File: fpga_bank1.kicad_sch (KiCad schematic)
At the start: 2 parts, among them U2 XC7A50T-FGG484

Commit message: Schematic finished, starting layout
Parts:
- added C33, C40, C55, C56, C57, C59, C60, C61, C62, C63, C64: 100n, Capacitor_SMD:C_0402_1005Metric_Pad0.74x0.62mm_HandSolder, symbol Device:C_Small
- added C54, C65: 4.7u, Capacitor_SMD:C_0402_1005Metric_Pad0.74x0.62mm_HandSolder, symbol Device:C_Small
- R12: renamed from R1; footprint Resistor_SMD:R_0603_1608Metric_Pad0.98x0.95mm_HandSolder -> Resistor_SMD:R_0402_1005Metric_Pad0.72x0.64mm_HandSolder; LCSC C21190 -> (none)
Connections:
- net +3V3: now also C33.2, C40.2, C54.2, C55.2, C56.2, C57.2, C59.2, C60.2, C61.2, C62.2, C63.2, C64.2, C65.2
- net FPGA_SPI0_CE0: now reaches U2.W19 (IO_L12P_T1_MRCC_14)
- net FPGA_SPI0_CE1: now reaches U2.W20 (IO_L12N_T1_MRCC_14)
- net SPI0_SCK: now reaches U2.Y18 (IO_L13P_T2_MRCC_14)
- new net GND: C33.1, C40.1, C54.1, C55.1, C56.1, C57.1, C59.1, C60.1, C61.1, C62.1, C63.1, C64.1, C65.1
- no-connect marks 0 -> 44
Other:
- note added: "(data output for serial daisy chains)"
- note added: "(serial configuration data input)"
- note added: "Nothing specific here. On MRCC pins for just in case."
- title: FPGA Bank 14 -> FPGA Power
- moved on the sheet: R12, U2A

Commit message: Updated titleblock texts
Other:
- title: FPGA Power -> FPGA Bank 14
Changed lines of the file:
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@@
   (paper "A4")
   (title_block
-    (title "FPGA Power")
-    (date "2024-02-11")
+    (title "FPGA Bank 14")
+    (date "2024-02-14")
     (rev "0.1")
     (company "George Smart, M1GEO")

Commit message: Started routing. More to go
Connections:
- net FPGA_SPI0_CE0 renamed FPGA_PI_GPIO8
- net FPGA_SPI0_CE1 renamed FPGA_PI_GPIO7
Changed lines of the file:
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@@
     (effects (font (size 1.27 1.27)) (justify left bottom))
   )
-  (hierarchical_label "FPGA_SPI0_CE1" (shape input) (at 127 106.045 0) (fields_autoplaced)
+  (hierarchical_label "FPGA_PI_GPIO7" (shape input) (at 127 106.045 0) (fields_autoplaced)
     (effects (font (size 1.27 1.27)) (justify left))
   )
@@
     (effects (font (size 1.27 1.27)) (justify left))
   )
-  (hierarchical_label "FPGA_SPI0_CE0" (shape input) (at 127 103.505 0) (fields_autoplaced)
+  (hierarchical_label "FPGA_PI_GPIO8" (shape input) (at 127 103.505 0) (fields_autoplaced)
     (effects (font (size 1.27 1.27)) (justify left))
   )

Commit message: More routing and tinkering. Need to do non-MGT decoupling next.
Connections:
- net FPGA_PI_GPIO7: no longer names the net of U2.W20 (IO_L12N_T1_MRCC_14)
- net FPGA_PI_GPIO8: no longer names the net of U2.W19 (IO_L12P_T1_MRCC_14)
- no-connect marks 44 -> 46
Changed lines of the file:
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@@
   (no_connect (at 111.76 141.605))
   (no_connect (at 111.76 159.385))
+  (no_connect (at 111.76 103.505))
   (no_connect (at 111.76 136.525))
   (no_connect (at 111.76 118.745))
@@
   (no_connect (at 111.76 85.725))
   (no_connect (at 111.76 60.325))
+  (no_connect (at 111.76 106.045))
   (no_connect (at 111.76 111.125))
   (no_connect (at 111.76 78.105))
@@
     (stroke (width 0) (type default))
   )
-  (wire (pts (xy 111.76 108.585) (xy 127 108.585))
-    (stroke (width 0) (type default))
-  )
   (wire (pts (xy 36.83 183.515) (xy 36.83 182.245))
     (stroke (width 0) (type default))
@@
     (stroke (width 0) (type default))
   )
-  (wire (pts (xy 111.76 106.045) (xy 127 106.045))
-    (stroke (width 0) (type default))
-  )
   (wire (pts (xy 21.59 188.595) (xy 21.59 189.23))
     (stroke (width 0) (type default))
@@
     (stroke (width 0) (type default))
   )
-  (wire (pts (xy 111.76 103.505) (xy 127 103.505))
-    (stroke (width 0) (type default))
-  )
   (wire (pts (xy 41.91 188.595) (xy 41.91 189.23))
+    (stroke (width 0) (type default))
+  )
+  (wire (pts (xy 111.76 108.585) (xy 116.205 108.585))
     (stroke (width 0) (type default))
   )
@@
   )
   (text "Nothing specific here.\nOn MRCC pins for just in case."
-    (at 147.32 107.95 0)
+    (at 128.905 110.49 0)
     (effects (font (size 1.27 1.27)) (justify left bottom))
   )
@@
     (effects (font (size 1.27 1.27)) (justify left bottom))
   )
-  (hierarchical_label "FPGA_PI_GPIO7" (shape input) (at 127 106.045 0) (fields_autoplaced)
-    (effects (font (size 1.27 1.27)) (justify left))
-  )
   (hierarchical_label "FPGA_PROG_MOSI" (shape input) (at 127 50.165 0) (fields_autoplaced)
     (effects (font (size 1.27 1.27)) (justify left))
   )
-  (hierarchical_label "FPGA_PI_GPIO8" (shape input) (at 127 103.505 0) (fields_autoplaced)
-    (effects (font (size 1.27 1.27)) (justify left))
-  )
   (hierarchical_label "FPGA_PROG_MISO" (shape output) (at 127 121.285 0) (fields_autoplaced)
     (effects (font (size 1.27 1.27)) (justify left))
   )
-  (hierarchical_label "SPI0_SCK" (shape input) (at 127 108.585 0) (fields_autoplaced)
+  (hierarchical_label "SPI0_SCK" (shape input) (at 116.205 108.585 0) (fields_autoplaced)
     (effects (font (size 1.27 1.27)) (justify left))
   )

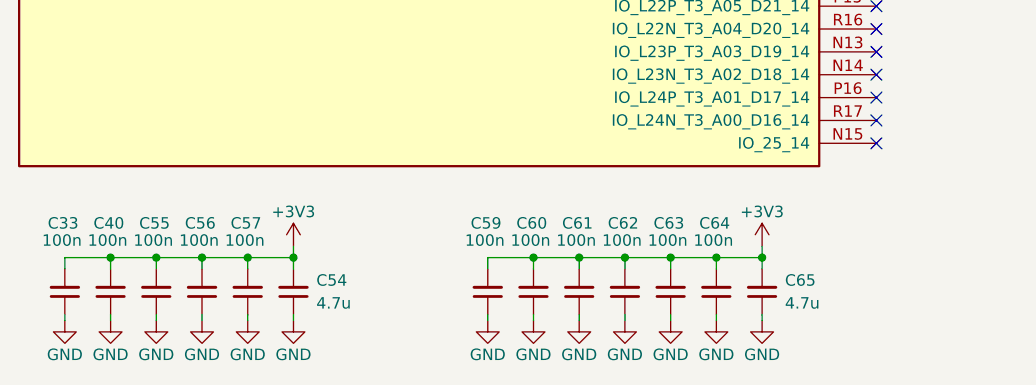
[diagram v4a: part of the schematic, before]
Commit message: Updated decoupling. Need to work out larger planes and fills.
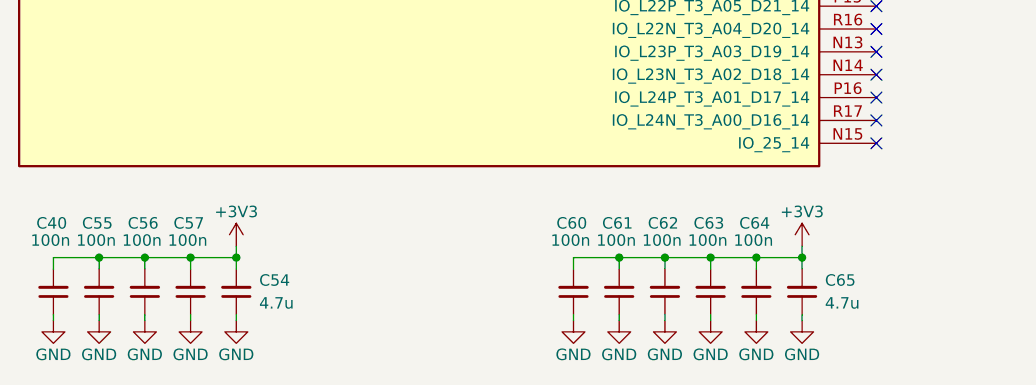
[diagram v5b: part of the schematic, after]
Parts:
- removed C33, C59: 100n, Capacitor_SMD:C_0402_1005Metric_Pad0.74x0.62mm_HandSolder, symbol Device:C_Small
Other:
- moved on the sheet: C40, C54, C55, C56, C57, C60, C61, C62, C63, C64, C65

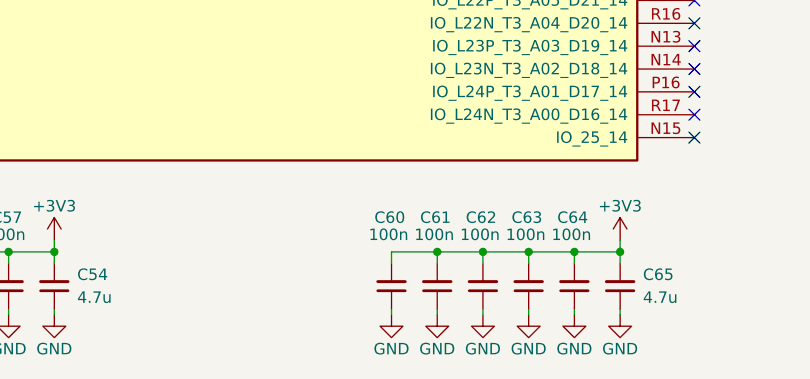
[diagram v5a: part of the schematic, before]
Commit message: Routing finished; Need to battle through the DRCs now. There's a few!
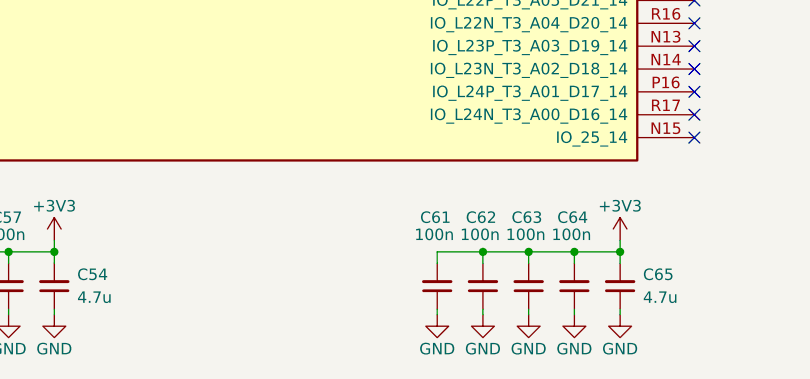
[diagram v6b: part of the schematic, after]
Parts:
- removed C60: 100n, Capacitor_SMD:C_0402_1005Metric_Pad0.74x0.62mm_HandSolder, symbol Device:C_Small
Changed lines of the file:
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@@
   (junction (at 27.94 22.225) (diameter 0) (color 0 0 0 0)
-  )
-  (junction (at 83.185 182.245) (diameter 0) (color 0 0 0 0)
   )
   (junction (at 96.52 22.225) (diameter 0) (color 0 0 0 0)
@@
     (stroke (width 0) (type default))
   )
-  (wire (pts (xy 78.105 183.515) (xy 78.105 182.245))
-    (stroke (width 0) (type default))
-  )
   (wire (pts (xy 25.4 182.245) (xy 30.48 182.245))
     (stroke (width 0) (type default))
@@
     (stroke (width 0) (type default))
   )
-  (wire (pts (xy 78.105 182.245) (xy 83.185 182.245))
-    (stroke (width 0) (type default))
-  )
   (wire (pts (xy 123.19 34.925) (xy 123.19 37.465))
-    (stroke (width 0) (type default))
-  )
-  (wire (pts (xy 78.105 188.595) (xy 78.105 189.23))
     (stroke (width 0) (type default))
   )
@@
     )
   )
-  (symbol (lib_id "power:GND") (at 78.105 189.23 0) (unit 1)
-    (in_bom yes) (on_board yes) (dnp no)
-    (property "Reference" "#PWR099" (at 78.105 195.58 0)
-      (effects (font (size 1.27 1.27)) hide)
-    )
-    (property "Value" "GND" (at 78.105 193.04 0)
-      (effects (font (size 1.27 1.27)))
-    )
-    (property "Footprint" "" (at 78.105 189.23 0)
-      (effects (font (size 1.27 1.27)) hide)
-    )
-    (property "Datasheet" "" (at 78.105 189.23 0)
-      (effects (font (size 1.27 1.27)) hide)
-    )
-    (pin "1")
-    (instances
-      (project "Pi5-Artix50T-Hat"
-        (path "/e63e39d7-6ac0-4ffd-8aa3-1841a4541b55/58f29d61-b732-4149-afb6-3ea37966fd1b/c8a6c160-0c2e-4b8d-861e-a10dfd0e8d60"
-          (reference "#PWR099") (unit 1)
-        )
-      )
-    )
-  )
   (symbol (lib_id "power:GND") (at 93.345 189.23 0) (unit 1)
     (in_bom yes) (on_board yes) (dnp no)
@@
         )
       )
-    )
-  )
-  (symbol (lib_id "Device:C_Small") (at 78.105 186.055 180) (unit 1)
-    (in_bom yes) (on_board yes) (dnp no)
-    (property "Reference" "C60" (at 76.2 178.435 0)
-      (effects (font (size 1.27 1.27)) (justify right))
-    )
-    (property "Value" "100n" (at 75.565 180.34 0)
-      (effects (font (size 1.27 1.27)) (justify right))
-    )
-    (property "Footprint" "Capacitor_SMD:C_0402_1005Metric_Pad0.74x0.62mm_HandSolder" (at 78.105 186.055 0)
-      (effects (font (size 1.27 1.27)) hide)
-    )
-    (property "Datasheet" "https://datasheet.lcsc.com/lcsc/2304140030_Samsung-Electro-Mechanics-CL05B104KO5NNNC_C1525.pdf" (at 78.105 186.055 0)
-      (effects (font (size 1.27 1.27)) hide)
-    )
-    (property "LCSC" "C1525" (at 78.105 186.055 90)
-      (effects (font (size 1.27 1.27)) hide)
-    )
-    (pin "2")
-    (pin "1")
-    (instances
-      (project "Pi5-Artix50T-Hat"
-        (path "/e63e39d7-6ac0-4ffd-8aa3-1841a4541b55/58f29d61-b732-4149-afb6-3ea37966fd1b/c8a6c160-0c2e-4b8d-861e-a10dfd0e8d60"
-          (reference "C60") (unit 1)
-        )
-      )

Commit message: Ordered boards from JLCPCB for V1
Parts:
- C40, C54, C55, C56, C57, C61, C62, C63, C64, C65: footprint Capacitor_SMD:C_0402_1005Metric_Pad0.74x0.62mm_HandSolder -> Capacitor_SMD:C_0402_1005Metric
- R12: footprint Resistor_SMD:R_0402_1005Metric_Pad0.72x0.64mm_HandSolder -> Resistor_SMD:R_0402_1005Metric; LCSC (none) -> C11702
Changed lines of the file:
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@@
       (effects (font (size 1.27 1.27)) (justify left))
     )
-    (property "Footprint" "Resistor_SMD:R_0402_1005Metric_Pad0.72x0.64mm_HandSolder" (at 123.19 40.005 0)
-      (effects (font (size 1.27 1.27)) hide)
-    )
-    (property "Datasheet" "" (at 123.19 40.005 0)
-      (effects (font (size 1.27 1.27)) hide)
-    )
-    (property "LCSC" "" (at 123.19 40.005 0)
+    (property "Footprint" "Resistor_SMD:R_0402_1005Metric" (at 123.19 40.005 0)
+      (effects (font (size 1.27 1.27)) hide)
+    )
+    (property "Datasheet" "https://datasheet.lcsc.com/lcsc/2206010216_UNI-ROYAL-Uniroyal-Elec-0402WGF1001TCE_C11702.pdf" (at 123.19 40.005 0)
+      (effects (font (size 1.27 1.27)) hide)
+    )
+    (property "LCSC" "C11702" (at 123.19 40.005 0)
       (effects (font (size 1.27 1.27)) hide)
     )
@@
       (effects (font (size 1.27 1.27)) (justify right))
     )
-    (property "Footprint" "Capacitor_SMD:C_0402_1005Metric_Pad0.74x0.62mm_HandSolder" (at 88.265 186.055 0)
+    (property "Footprint" "Capacitor_SMD:C_0402_1005Metric" (at 88.265 186.055 0)
       (effects (font (size 1.27 1.27)) hide)
     )
@@
       (effects (font (size 1.27 1.27)) (justify right))
     )
-    (property "Footprint" "Capacitor_SMD:C_0402_1005Metric_Pad0.74x0.62mm_HandSolder" (at 83.185 186.055 0)
+    (property "Footprint" "Capacitor_SMD:C_0402_1005Metric" (at 83.185 186.055 0)
       (effects (font (size 1.27 1.27)) hide)
     )
@@
       (effects (font (size 1.27 1.27)) (justify right))
     )
-    (property "Footprint" "Capacitor_SMD:C_0402_1005Metric_Pad0.74x0.62mm_HandSolder" (at 25.4 186.055 0)
+    (property "Footprint" "Capacitor_SMD:C_0402_1005Metric" (at 25.4 186.055 0)
       (effects (font (size 1.27 1.27)) hide)
     )
@@
       (effects (font (size 1.27 1.27)) (justify right))
     )
-    (property "Footprint" "Capacitor_SMD:C_0402_1005Metric_Pad0.74x0.62mm_HandSolder" (at 40.64 186.055 0)
+    (property "Footprint" "Capacitor_SMD:C_0402_1005Metric" (at 40.64 186.055 0)
       (effects (font (size 1.27 1.27)) hide)
     )
@@
       (effects (font (size 1.27 1.27)) (justify right))
     )
-    (property "Footprint" "Capacitor_SMD:C_0402_1005Metric_Pad0.74x0.62mm_HandSolder" (at 20.32 186.055 0)
+    (property "Footprint" "Capacitor_SMD:C_0402_1005Metric" (at 20.32 186.055 0)
       (effects (font (size 1.27 1.27)) hide)
     )
@@
       (effects (font (size 1.27 1.27)) (justify right))
     )
-    (property "Footprint" "Capacitor_SMD:C_0402_1005Metric_Pad0.74x0.62mm_HandSolder" (at 30.48 186.055 0)
+    (property "Footprint" "Capacitor_SMD:C_0402_1005Metric" (at 30.48 186.055 0)
       (effects (font (size 1.27 1.27)) hide)
     )
@@
       (effects (font (size 1.27 1.27)) (justify right))
     )
-    (property "Footprint" "Capacitor_SMD:C_0402_1005Metric_Pad0.74x0.62mm_HandSolder" (at 103.505 186.055 0)
+    (property "Footprint" "Capacitor_SMD:C_0402_1005Metric" (at 103.505 186.055 0)
       (effects (font (size 1.27 1.27)) hide)
     )
@@
       (effects (font (size 1.27 1.27)) (justify right))
     )
-    (property "Footprint" "Capacitor_SMD:C_0402_1005Metric_Pad0.74x0.62mm_HandSolder" (at 93.345 186.055 0)
+    (property "Footprint" "Capacitor_SMD:C_0402_1005Metric" (at 93.345 186.055 0)
       (effects (font (size 1.27 1.27)) hide)
     )
@@
       (effects (font (size 1.27 1.27)) (justify right))
     )
-    (property "Footprint" "Capacitor_SMD:C_0402_1005Metric_Pad0.74x0.62mm_HandSolder" (at 35.56 186.055 0)
+    (property "Footprint" "Capacitor_SMD:C_0402_1005Metric" (at 35.56 186.055 0)
       (effects (font (size 1.27 1.27)) hide)
     )
@@
       (effects (font (size 1.27 1.27)) (justify right))
     )
-    (property "Footprint" "Capacitor_SMD:C_0402_1005Metric_Pad0.74x0.62mm_HandSolder" (at 98.425 186.055 0)
-      (effects (font (size 1.27 1.27)) hide)
-    )
+    (property "Footprint" "Capacitor_SMD:C_0402_1005Metric" (at 98.425 186.055 0)
+      (effects (font (size 1.27 1.27)) hide)
+    )
